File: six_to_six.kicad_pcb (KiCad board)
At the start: 2 copper layers, 99.8 x 77.5 mm, 73 parts, among them J1 RF Conn, J2 limiter, J3 Relay control, J7 BNC, K1 RY-12W-K, K2 RY-12W-K, K3 RY-12W-K, K4 RY-12W-K, K5 RY-12W-K, K6 RY-12W-K, Q1 MMBT3904, Q2 MMBT3904, Q3 MMBT3904, Q4 MMBT3904, Q5 MMBT3904, Q6 MMBT3904

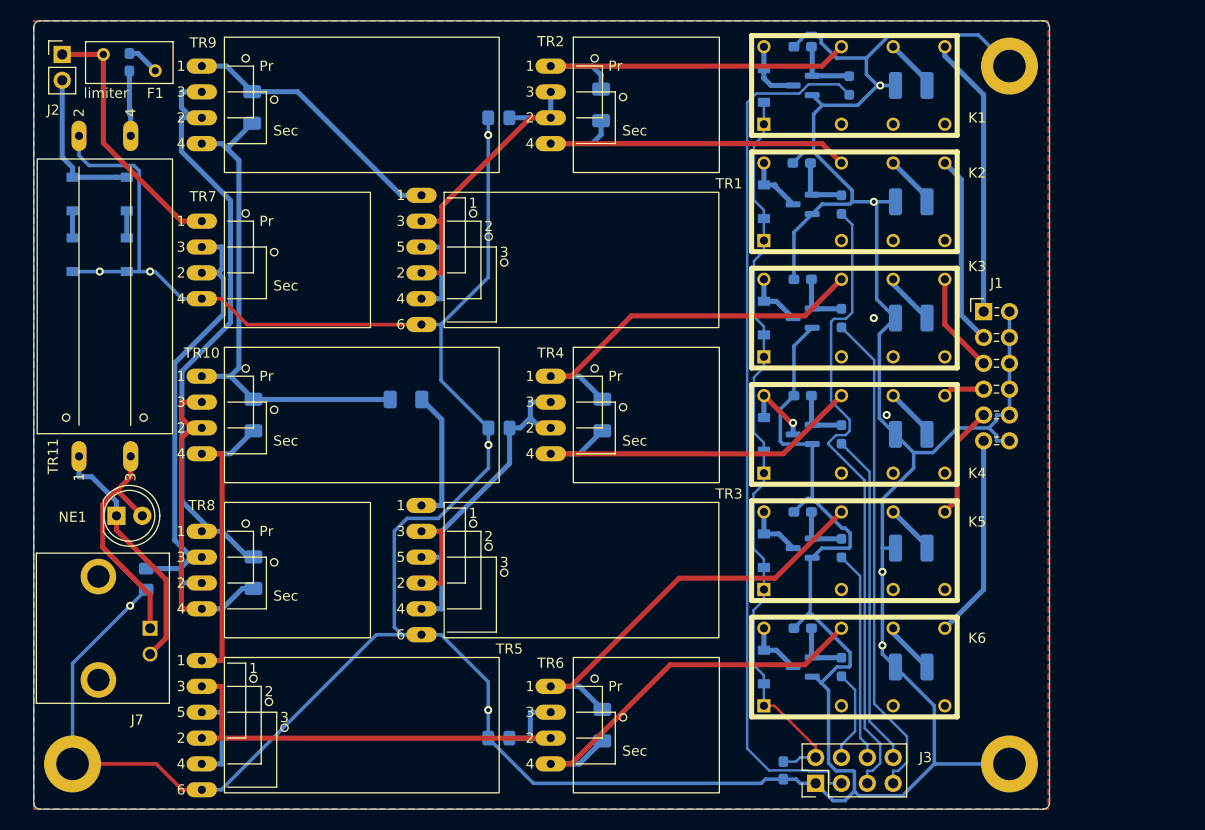
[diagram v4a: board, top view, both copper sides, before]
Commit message: changed footprint for 2-way splitter transformer
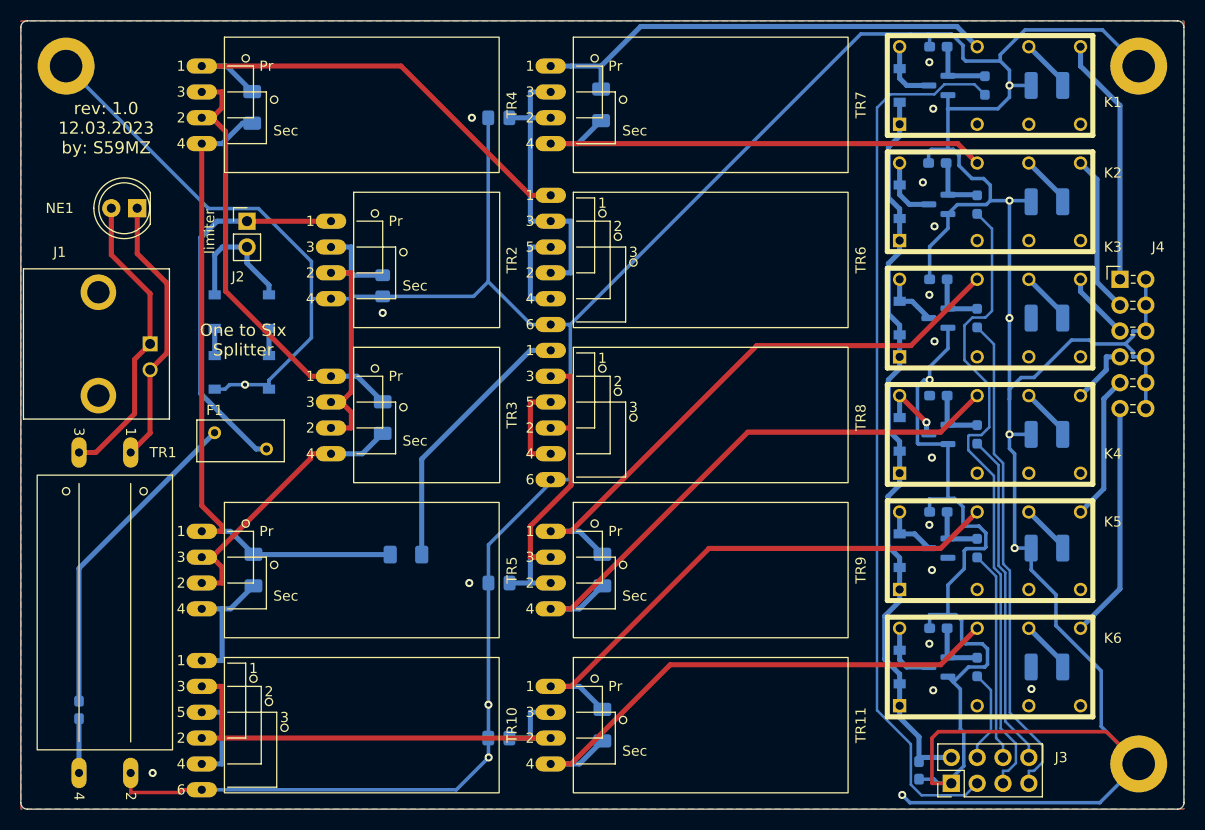
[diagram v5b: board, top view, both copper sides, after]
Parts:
- TR11: renamed from TR6; footprint Components:BN-73-202-2-0 -> Components:BN-73-6802-2-0
- TR7: renamed from TR2; footprint Components:BN-73-202-2-0 -> Components:BN-73-6802-2-0
- TR9: renamed from TR4; footprint Components:BN-73-202-2-0 -> Components:BN-73-6802-2-0
- moved H1 68.6 mm to (645.8, 163.8)
- moved C7 63.8 mm to (647.1, 227.1)
- moved C8 37.0 mm to (676.9, 185.4)
- moved F1 36.0 mm to (660.4, 199.9), turned to 0 degrees
- moved NE1 30.3 mm to (652.8, 177.8), turned to 180 degrees
- moved J1 27.9 mm to (649.0, 191.1)
- moved J2 24.5 mm to (663.6, 179.1)
- moved TR3 19.8 mm to (671.8, 194.3)
- moved R13 19.8 mm to (676.9, 198.4)
- moved TR8 19.8 mm to (693.4, 191.8)
- moved D7 18.1 mm to (665.7, 188.0)
- moved D9 18.1 mm to (660.4, 188.0)
- moved D10 18.1 mm to (660.4, 193.9)
- moved D8 18.1 mm to (665.7, 193.9)
- moved C10 15.2 mm to (688.3, 214.6)
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- renumbered C8 to C10, C9 to C11, C10 to C7, C11 to C8, C7 to C9, D9 to D10, D10 to D7, D7 to D8, D8 to D9, J7 to J1, J1 to J4, R16 to R13, R17 to R14, R18 to R15, R19 to R16, R13 to R17, R14 to R18, R15 to R19, TR11 to TR1, TR5 to TR10, TR7 to TR2, TR8 to TR3, TR9 to TR4, TR10 to TR5, TR1 to TR6, TR3 to TR8
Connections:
- net /One to Six splitter/2-Way Splitter1/RF-in renamed /2-Way Splitter1/RF-in
- net /One to Six splitter/2-Way Splitter1/RF-out-1 renamed /2-Way Splitter1/RF-out-1
- net /One to Six splitter/2-Way Splitter1/RF-out-2 renamed /2-Way Splitter1/RF-out-2
- net /One to Six splitter/2-Way Splitter2/RF-in renamed /2-Way Splitter2/RF-in
- net /One to Six splitter/2-Way Splitter2/RF-out-1 renamed /2-Way Splitter2/RF-out-1
- net /One to Six splitter/2-Way Splitter2/RF-out-2 renamed /2-Way Splitter2/RF-out-2
- net /One to Six splitter/2-Way Splitter3/RF-in renamed /2-Way Splitter3/RF-in
- net /One to Six splitter/2-Way Splitter3/RF-out-1 renamed /2-Way Splitter3/RF-out-1
- net /One to Six splitter/2-Way Splitter3/RF-out-2 renamed /2-Way Splitter3/RF-out-2
- net /One to Six splitter/3-Way Splitter/RF-in renamed /3-Way Splitter/RF-in
- net /One to Six splitter/Connectors/RF-1 renamed /Connectors/RF-1
- net /One to Six splitter/Connectors/RF-2 renamed /Connectors/RF-2
- net /One to Six splitter/Connectors/RF-3 renamed /Connectors/RF-3
- net /One to Six splitter/Connectors/RF-4 renamed /Connectors/RF-4
- net /One to Six splitter/Connectors/RF-5 renamed /Connectors/RF-5
- net /One to Six splitter/Connectors/RF-6 renamed /Connectors/RF-6
- net /One to Six splitter/Connectors/Relay-1 renamed /Connectors/Relay-1
- net /One to Six splitter/Connectors/Relay-2 renamed /Connectors/Relay-2
- net /One to Six splitter/Connectors/Relay-3 renamed /Connectors/Relay-3
- net /One to Six splitter/Connectors/Relay-4 renamed /Connectors/Relay-4
- net /One to Six splitter/Connectors/Relay-5 renamed /Connectors/Relay-5
- net /One to Six splitter/Connectors/Relay-6 renamed /Connectors/Relay-6
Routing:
- net GND: track 469.8 -> 519.2 mm, vias 12 -> 26
- net Net-(C7-Pad2): track 3.24 -> 31.9 mm
- net /2-Way Splitter2/RF-out-1: track 38.5 -> 58.2 mm
- net /2-Way Splitter2/RF-out-2: track 37.0 -> 56.6 mm
- net /2-Way Splitter1/RF-in: track 26.9 -> 45.5 mm
- net Net-(R14-Pad2): track 48.9 -> 66.2 mm
- net /2-Way Splitter3/RF-in: track 30.3 -> 13.1 mm
- net Net-(C8-Pad1): track 46.5 -> 30.8 mm
- net Net-(R13-Pad1): track 58.9 -> 43.5 mm
- net /2-Way Splitter3/RF-out-2: track 40.1 -> 53.4 mm
- net /2-Way Splitter3/RF-out-1: track 41.7 -> 55.0 mm
- net /2-Way Splitter2/RF-in: track 13.2 -> 26.5 mm
- net /2-Way Splitter1/RF-out-2: track 36.1 -> 48.6 mm
- net /3-Way Splitter/RF-in: track 25.6 -> 37.5 mm
- net /2-Way Splitter1/RF-out-1: track 36.1 -> 46.6 mm
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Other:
- board size 99.8 x 77.5 mm -> 114.3 x 77.5 mm
- board text added: "One to Six Splitter"
- board text added: "rev: 1.0 12.03.2023 by: S59MZ"
- board text removed: "six to six splitter/combiner rev: 1.0 12.03.2023 designed by: S59MZ"
